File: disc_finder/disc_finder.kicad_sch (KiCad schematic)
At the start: 12 parts, among them J1 Battery, Q1 DMN6140L-7, U1 ICM7555xB

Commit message: Increased 555 timer frequency so that buzzer is audible, and delayed initial operation using RC
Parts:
- added C3: 10u, Capacitor_SMD:C_0603_1608Metric, symbol Device:C
- added Q2: DMN6140L-7, Package_TO_SOT_SMD:TSOT-23, symbol Device:Q_NMOS_GSD
- added R5: 10M, Resistor_SMD:R_0603_1608Metric, symbol Device:R
- C1: value 1u -> 0.1u; Voltage 16V -> 50V; mpn C_0603_1u_16V_X7R -> C_0603_0.1u_50V_X7R
- R3: value 1M -> 1k; mpn R_0603_1M_1% -> R_0603_1k_1%
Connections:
- net GND: now also C3.2, Q2.2 (S); no longer Q1.2 (S)
- net VDD: now also R5.1
- new net: Q1.2 (S), Q2.3 (D)
- new net: C3.1, Q2.1 (G), R5.2
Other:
- note added: "Delay the operation of the buzzer/LED 10M/10u = 100s But cap will be <10u due to dc bias"
- note added: "f = 1.44/((0 + 2*1*10^3)*0.1*10^-6) = 7200 Hz"
- note removed: "f = 1.44/((0 + 2*1*10^6)*1*10^-6) = 0.72 Hz"

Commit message: Now using a bright orange LED, and moved it to the middle of the board
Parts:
- D1: footprint LED_SMD:LED_0603_1608Metric -> disc:LED_OSRAM_TOPLED
- R4: value 330R -> 100R; mpn R_0603_330R_5% -> R_0603_100R_1%
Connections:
- net VDD: now also D1.2 (A); no longer R4.1
- net at BZ1.2 (-), Q1.3 (D): now also R4.2; no longer D1.1 (K)
- new net: D1.1 (K), R4.1
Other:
- note added: "Adjust as required"
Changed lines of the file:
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@@
+		)
+	)
+	(text "Adjust as required"
+		(exclude_from_sim no)
+		(at 254.254 44.45 0)
+		(effects
+			(font
+				(size 1.27 1.27)
+			)
 		)
 	)
@@
 	(symbol
 		(lib_id "Device:R")
-		(at 243.84 35.56 0)
-		(mirror y)
-		(unit 1)
-		(exclude_from_sim no)
-		(in_bom yes)
-		(on_board yes)
-		(dnp no)
-		(property "Reference" "R4"
-			(at 241.3 35.56 90)
-			(effects
-				(font
-					(size 1.27 1.27)
-				)
-			)
-		)
-		(property "Value" "330R"
-			(at 243.84 35.56 90)
-			(effects
-				(font
-					(size 1.27 1.27)
-				)
-			)
-		)
-		(property "Footprint" "Resistor_SMD:R_0603_1608Metric"
-			(at 245.618 35.56 90)
-			(effects
-				(font
-					(size 1.27 1.27)
-				)
-				(hide yes)
-			)
-		)
-		(property "Datasheet" "~"
-			(at 243.84 35.56 0)
-			(effects
-				(font
-					(size 1.27 1.27)
-				)
-				(hide yes)
-			)
-		)
-		(property "Description" "Resistor"
-			(at 243.84 35.56 0)
-			(effects
-				(font
-					(size 1.27 1.27)
-				)
-				(hide yes)
-			)
-		)
-		(property "mpn" "R_0603_330R_5%"
-			(at 243.84 35.56 90)
-			(effects
-				(font
-					(size 1.27 1.27)
-				)
-				(hide yes)
-			)
-		)
-		(pin "1"
-		)
-		(pin "2"
-		)
-		(instances
-			(project "disc_finder"
-				(path "/bc8f2379-d0e7-4939-b0df-9bb187dda8ee"
-					(reference "R4")
-					(unit 1)
-				)
-			)
-		)
-	)
-	(symbol
-		(lib_id "Device:R")
 		(at 156.21 74.93 90)
 		(unit 1)
@@
 	)
 	(symbol
+		(lib_id "Device:R")
+		(at 243.84 43.18 0)
+		(mirror y)
+		(unit 1)
+		(exclude_from_sim no)
+		(in_bom yes)
+		(on_board yes)
+		(dnp no)
+		(property "Reference" "R4"
+			(at 241.3 43.18 90)
+			(effects
+				(font
+					(size 1.27 1.27)
+				)
+			)
+		)
+		(property "Value" "100R"
+			(at 243.84 43.18 90)
+			(effects
+				(font
+					(size 1.27 1.27)
+				)
+			)
+		)
+		(property "Footprint" "Resistor_SMD:R_0603_1608Metric"
+			(at 245.618 43.18 90)
+			(effects
+				(font
+					(size 1.27 1.27)
+				)
+				(hide yes)
+			)
+		)
+		(property "Datasheet" "~"
+			(at 243.84 43.18 0)
+			(effects
+				(font
+					(size 1.27 1.27)
+				)
+				(hide yes)
+			)
+		)
+		(property "Description" "Resistor"
+			(at 243.84 43.18 0)
+			(effects
+				(font
+					(size 1.27 1.27)
+				)
+				(hide yes)
+			)
+		)
+		(property "mpn" "R_0603_100R_1%"
+			(at 243.84 43.18 90)
+			(effects
+				(font
+					(size 1.27 1.27)
+				)
+				(hide yes)
+			)
+		)
+		(pin "1"
+		)
+		(pin "2"
+		)
+		(instances
+			(project "disc_finder"
+				(path "/bc8f2379-d0e7-4939-b0df-9bb187dda8ee"
+					(reference "R4")
+					(unit 1)
+				)
+			)
+		)
+	)
+	(symbol
 		(lib_id "power:+BATT")
 		(at 22.86 29.21 0)
@@
 	(symbol
 		(lib_id "Device:LED")
-		(at 243.84 43.18 90)
+		(at 243.84 35.56 90)
 		(unit 1)
 		(exclude_from_sim no)
@@
 		(fields_autoplaced yes)
 		(property "Reference" "D1"
-			(at 247.65 43.4974 90)
+			(at 247.65 35.8774 90)
 			(effects
 				(font
@@
 		)
 		(property "Value" "LED"
-			(at 247.65 46.0374 90)
+			(at 247.65 38.4174 90)
 			(effects
 				(font
@@
 			)
 		)
-		(property "Footprint" "LED_SMD:LED_0603_1608Metric"
-			(at 243.84 43.18 0)
+		(property "Footprint" "disc:LED_OSRAM_TOPLED"
+			(at 243.84 35.56 0)
 			(effects
 				(font
@@
 		)
 		(property "Datasheet" "~"
-			(at 243.84 43.18 0)
+			(at 243.84 35.56 0)
 			(effects
 				(font
@@
 		)
 		(property "Description" "Light emitting diode"
-			(at 243.84 43.18 0)
+			(at 243.84 35.56 0)
 			(effects
 				(font
@@
 		)
 		(instances
-			(project ""
+			(project "disc_finder"
 				(path "/bc8f2379-d0e7-4939-b0df-9bb187dda8ee"
 					(reference "D1")

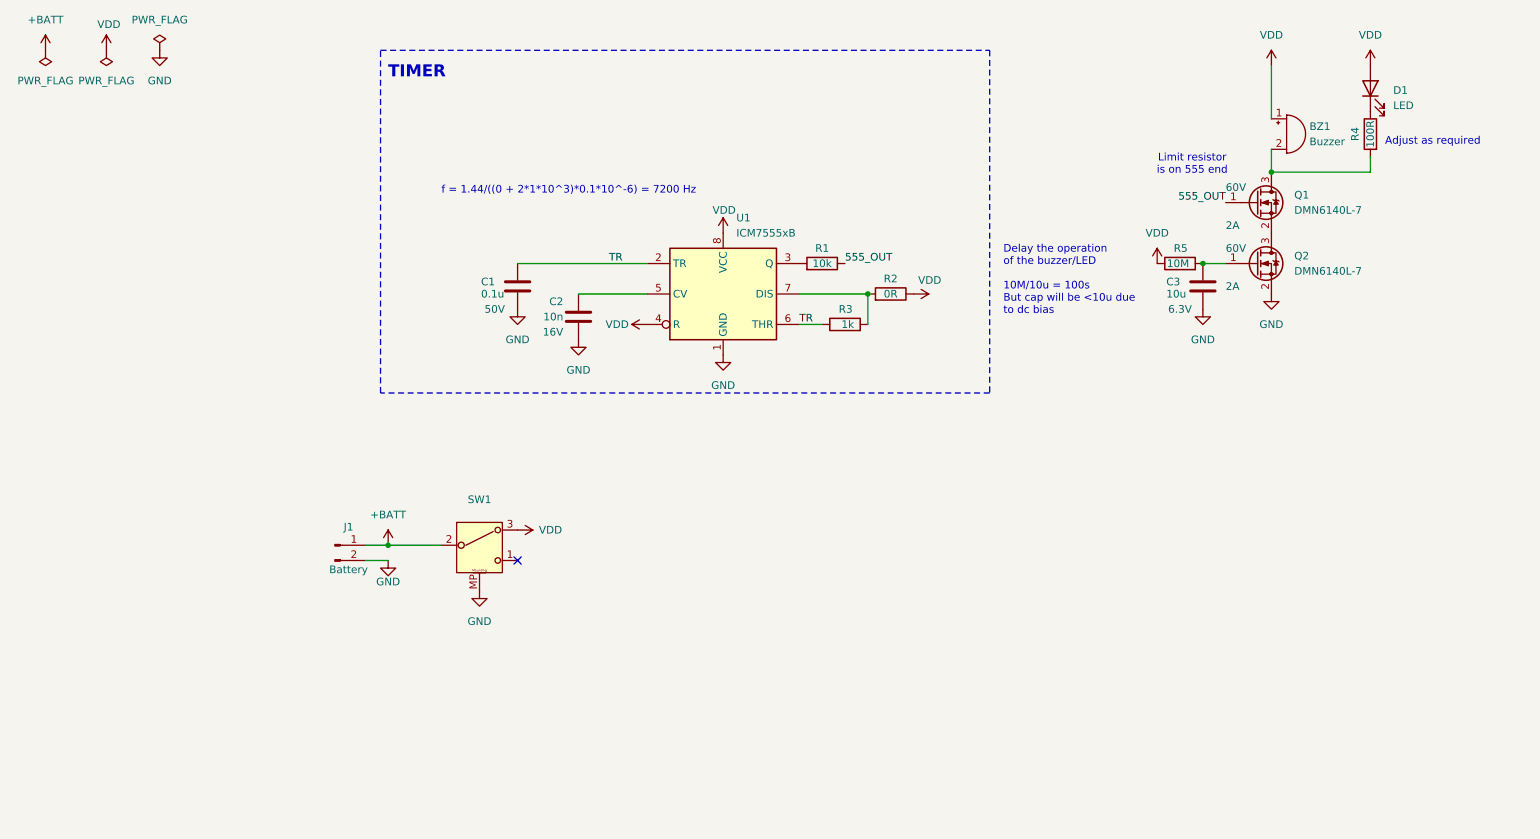
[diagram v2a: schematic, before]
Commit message: Added an additional 555 timer for the led
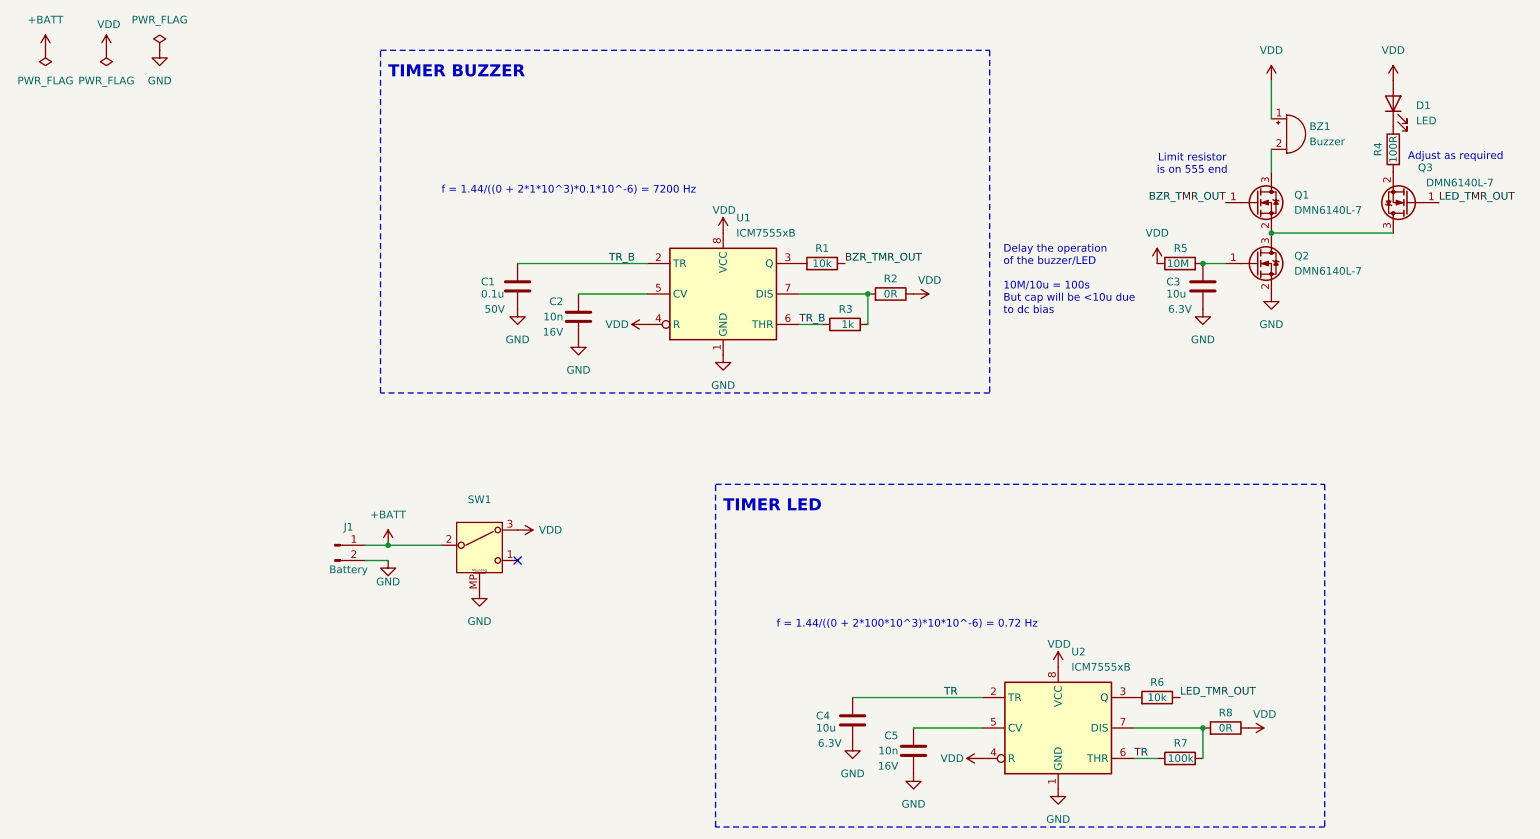
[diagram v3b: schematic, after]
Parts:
- added C4: 10u, Capacitor_SMD:C_0603_1608Metric, symbol Device:C
- added C5: 10n, Capacitor_SMD:C_0603_1608Metric, symbol Device:C
- added Q3: DMN6140L-7, Package_TO_SOT_SMD:TSOT-23, symbol Device:Q_NMOS_GSD
- added R6: 10k, Resistor_SMD:R_0603_1608Metric, symbol Device:R
- added R7: 100k, Resistor_SMD:R_0603_1608Metric, symbol Device:R
- added R8: 0R, Resistor_SMD:R_0603_1608Metric, symbol Device:R
- added U2: ICM7555xB, Package_SO:SOIC-8_3.9x4.9mm_P1.27mm, symbol Timer:ICM7555xB
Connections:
- net GND: now also C4.2, C5.2, U2.1 (GND)
- net TR: now also C4.1, R7.1, U2.2 (TR), U2.6 (THR); no longer C1.1, R3.1, U1.2 (TR), U1.6 (THR)
- net VDD: now also R8.1, U2.4 (R), U2.8 (VCC)
- net at Q1.2 (S), Q2.3 (D): now also Q3.3 (D)
- net at BZ1.2 (-), Q1.3 (D): no longer R4.2
- net 555_OUT renamed BZR_TMR_OUT
- new net: C5.1, U2.5 (CV)
- new net: Q3.2 (S), R4.2
- new net: R7.2, R8.2, U2.7 (DIS)
- new net: R6.2, U2.3 (Q)
- new net LED_TMR_OUT: Q3.1 (G), R6.1
- new net TR_B: C1.1, R3.1, U1.2 (TR), U1.6 (THR)
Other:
- note added: "TIMER BUZZER"
- note added: "TIMER LED"
- note added: "f = 1.44/((0 + 2*100*10^3)*10*10^-6) = 0.72 Hz"
- note removed: "TIMER"
- moved on the sheet: D1, R4

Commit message: Update kicad page vars with vars that are filled by kibot
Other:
- title: (none) -> ${title}
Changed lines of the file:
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@@
 	(generator_version "8.0")
 	(paper "A4")
+	(title_block
+		(title "${title}")
+		(date "${date}")
+		(rev "${rev}")
+	)
 	(junction
 		(at 160.02 69.85)

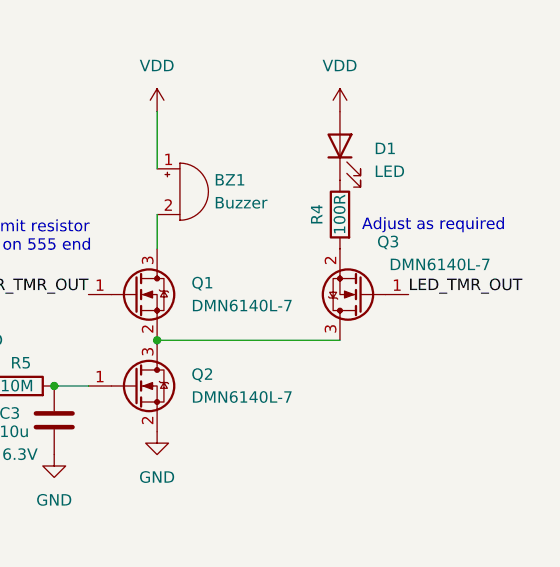
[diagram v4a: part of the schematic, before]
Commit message: Added battery holder step file and corrected LED nmos orientation
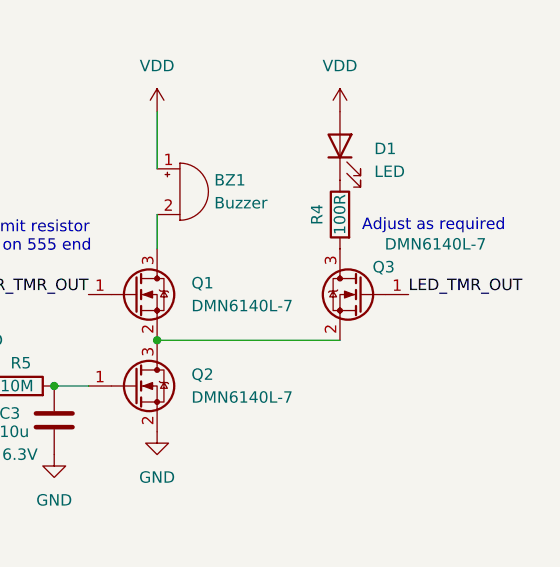
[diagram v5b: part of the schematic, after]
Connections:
- net at Q1.2 (S), Q2.3 (D): now also Q3.2 (S); no longer Q3.3 (D)
- net at R4.2: now also Q3.3 (D); no longer Q3.2 (S)
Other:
- moved on the sheet: Q3
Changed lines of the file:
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@@
 	(symbol
 		(lib_id "Device:Q_NMOS_GSD")
-		(at 250.19 54.61 180)
+		(at 250.19 54.61 0)
+		(mirror y)
 		(unit 1)
 		(exclude_from_sim no)
@@
 		(dnp no)
 		(property "Reference" "Q3"
-			(at 254.254 48.768 0)
+			(at 253.746 51.562 0)
 			(effects
 				(font
@@
 		)
 		(property "Value" "DMN6140L-7"
-			(at 264.414 51.308 0)
+			(at 263.906 49.022 0)
 			(effects
 				(font
@@
 		)
 		(property "Footprint" "Package_TO_SOT_SMD:TSOT-23"
-			(at 245.11 57.15 0)
+			(at 245.11 52.07 0)
 			(effects
 				(font
@@
 		)
 		(property "Voltage" "60V"
-			(at 255.27 57.15 0)
+			(at 255.27 52.07 0)
 			(effects
 				(font
@@
 		)
 		(property "Current" "2A"
-			(at 254.508 59.182 0)
+			(at 254.508 50.038 0)
 			(effects
 				(font
